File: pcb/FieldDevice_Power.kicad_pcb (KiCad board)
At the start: 2 copper layers, 22.9 x 20.6 mm, 12 parts, among them U1 LM2621

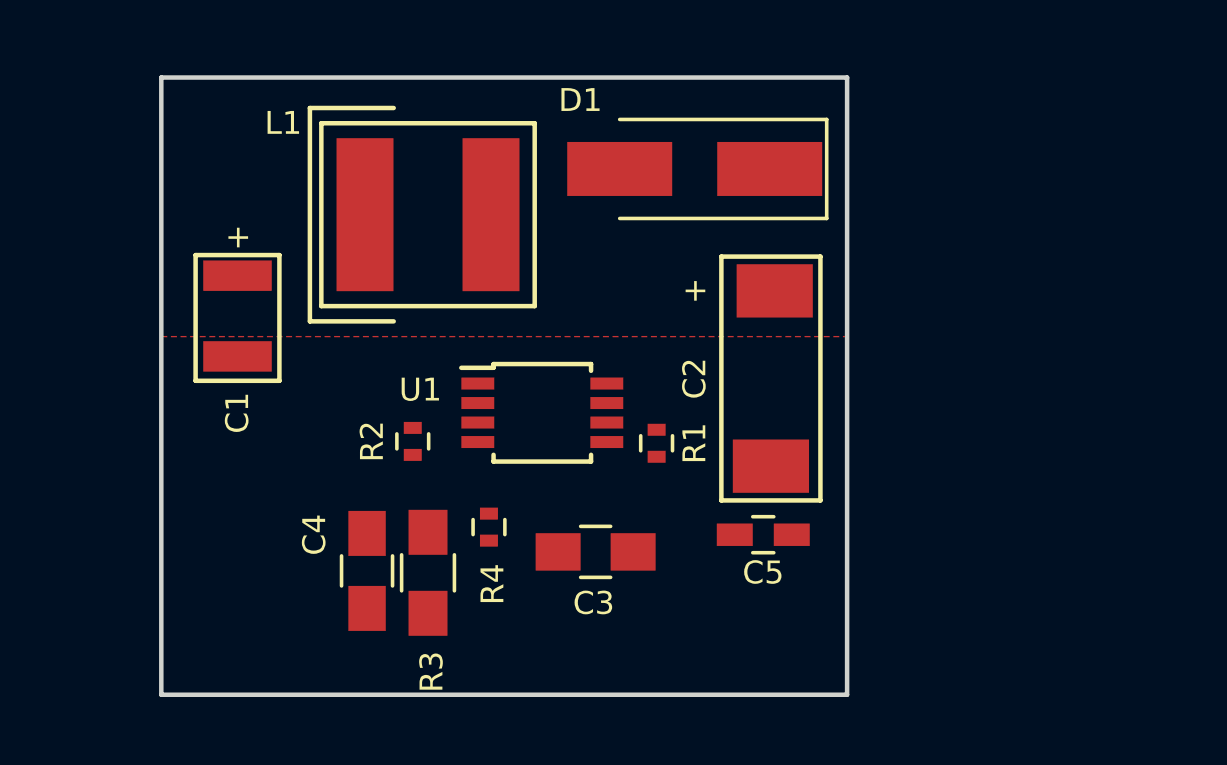
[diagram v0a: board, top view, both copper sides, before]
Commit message: Added the pin headers for Vin and Vout
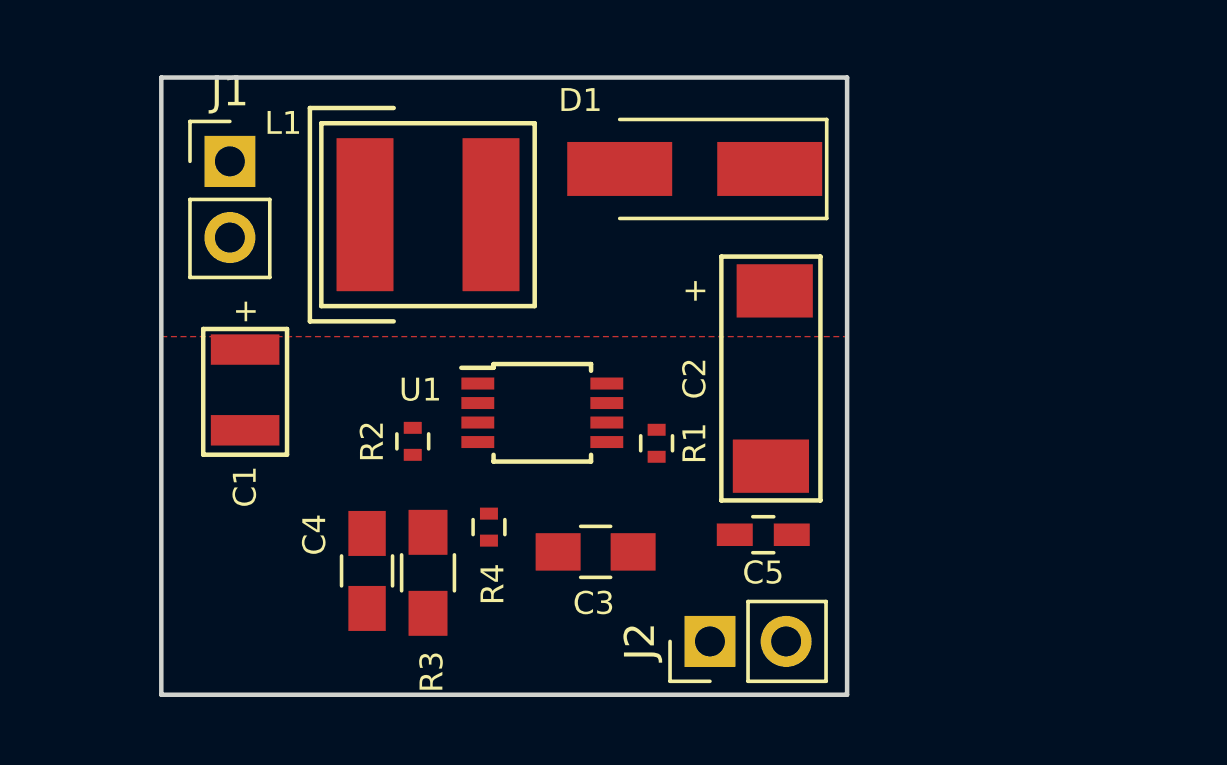
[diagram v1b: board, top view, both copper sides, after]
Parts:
- added J1: Vin, Pin_Headers:Pin_Header_Straight_1x02_Pitch2.54mm, F.Cu at (168.1, 98.8)
- added J2: Vout, Pin_Headers:Pin_Header_Straight_1x02_Pitch2.54mm, F.Cu at (184.2, 114.8)
- moved C1 2.48 mm to (168.7, 106.4)
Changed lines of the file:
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@@
 (kicad_pcb (version 4) (host pcbnew 4.0.7)
   (general
-    (links 23)
-    (no_connects 17)
-    (area 0 0 0 0)
+    (links 27)
+    (no_connects 22)
+    (area 165.786999 95.936999 188.797001 116.661001)
     (thickness 1.6)
     (drawings 4)
     (tracks 0)
     (zones 0)
-    (modules 12)
+    (modules 14)
     (nets 8)
   )
@@
     (pad_to_mask_clearance 0.2)
     (aux_axis_origin 0 0)
-    (visible_elements FFFEFF7F)
+    (visible_elements 7FFFFFFF)
     (pcbplotparams
       (layerselection 0x00030_80000001)
@@
   )
   (module FieldDevice_Power:Capacitor_1411 (layer F.Cu)
-    (at 168.402 103.9622 270)
+    (at 168.656 106.426 270)
     (fp_text reference C1 (at 3.2258 0 270) (layer F.SilkS)
       (effects (font (size 0.762 0.762) (thickness 0.127)))
@@
       (at (xyz 0 0 0))
       (scale (xyz 1 1 1))
+      (rotate (xyz 0 0 0))
+    )
+  )
+  (module Pin_Headers:Pin_Header_Straight_1x02_Pitch2.54mm (layer F.Cu)
+    (at 168.148 98.806)
+    (descr "Through hole straight pin header, 1x02, 2.54mm pitch, single row")
+    (tags "Through hole pin header THT 1x02 2.54mm single row")
+    (fp_text reference J1 (at 0 -2.33) (layer F.SilkS)
+      (effects (font (size 1 1) (thickness 0.15)))
+    )
+    (fp_text value Vin (at 0 4.87) (layer F.Fab)
+      (effects (font (size 1 1) (thickness 0.15)))
+    )
+    (fp_line (start -0.635 -1.27) (end 1.27 -1.27) (layer F.Fab) (width 0.1))
+    (fp_line (start 1.27 -1.27) (end 1.27 3.81) (layer F.Fab) (width 0.1))
+    (fp_line (start 1.27 3.81) (end -1.27 3.81) (layer F.Fab) (width 0.1))
+    (fp_line (start -1.27 3.81) (end -1.27 -0.635) (layer F.Fab) (width 0.1))
+    (fp_line (start -1.27 -0.635) (end -0.635 -1.27) (layer F.Fab) (width 0.1))
+    (fp_line (start -1.33 3.87) (end 1.33 3.87) (layer F.SilkS) (width 0.12))
+    (fp_line (start -1.33 1.27) (end -1.33 3.87) (layer F.SilkS) (width 0.12))
+    (fp_line (start 1.33 1.27) (end 1.33 3.87) (layer F.SilkS) (width 0.12))
+    (fp_line (start -1.33 1.27) (end 1.33 1.27) (layer F.SilkS) (width 0.12))
+    (fp_line (start -1.33 0) (end -1.33 -1.33) (layer F.SilkS) (width 0.12))
+    (fp_line (start -1.33 -1.33) (end 0 -1.33) (layer F.SilkS) (width 0.12))
+    (fp_line (start -1.8 -1.8) (end -1.8 4.35) (layer F.CrtYd) (width 0.05))
+    (fp_line (start -1.8 4.35) (end 1.8 4.35) (layer F.CrtYd) (width 0.05))
+    (fp_line (start 1.8 4.35) (end 1.8 -1.8) (layer F.CrtYd) (width 0.05))
+    (fp_line (start 1.8 -1.8) (end -1.8 -1.8) (layer F.CrtYd) (width 0.05))
+    (fp_text user %R (at 0 1.27 90) (layer F.Fab)
+      (effects (font (size 1 1) (thickness 0.15)))
+    )
+    (pad 1 thru_hole rect (at 0 0) (size 1.7 1.7) (drill 1) (layers *.Cu *.Mask)
+      (net 2 /Vin))
+    (pad 2 thru_hole oval (at 0 2.54) (size 1.7 1.7) (drill 1) (layers *.Cu *.Mask)
+      (net 1 GND))
+    (model ${KISYS3DMOD}/Pin_Headers.3dshapes/Pin_Header_Straight_1x02_Pitch2.54mm.wrl
+      (at (xyz 0 0 0))
+      (scale (xyz 1 1 1))
+      (rotate (xyz 0 0 0))
+    )
+  )
+  (module Pin_Headers:Pin_Header_Straight_1x02_Pitch2.54mm (layer F.Cu)
+    (at 184.15 114.808 90)
+    (descr "Through hole straight pin header, 1x02, 2.54mm pitch, single row")
+    (tags "Through hole pin header THT 1x02 2.54mm single row")
+    (fp_text reference J2 (at 0 -2.33 90) (layer F.SilkS)
+      (effects (font (size 1 1) (thickness 0.15)))
+    )
+    (fp_text value Vout (at 0 4.87 90) (layer F.Fab)
+      (effects (font (size 1 1) (thickness 0.15)))
+    )
+    (fp_line (start -0.635 -1.27) (end 1.27 -1.27) (layer F.Fab) (width 0.1))
+    (fp_line (start 1.27 -1.27) (end 1.27 3.81) (layer F.Fab) (width 0.1))
+    (fp_line (start 1.27 3.81) (end -1.27 3.81) (layer F.Fab) (width 0.1))
+    (fp_line (start -1.27 3.81) (end -1.27 -0.635) (layer F.Fab) (width 0.1))
+    (fp_line (start -1.27 -0.635) (end -0.635 -1.27) (layer F.Fab) (width 0.1))
+    (fp_line (start -1.33 3.87) (end 1.33 3.87) (layer F.SilkS) (width 0.12))
+    (fp_line (start -1.33 1.27) (end -1.33 3.87) (layer F.SilkS) (width 0.12))
+    (fp_line (start 1.33 1.27) (end 1.33 3.87) (layer F.SilkS) (width 0.12))
+    (fp_line (start -1.33 1.27) (end 1.33 1.27) (layer F.SilkS) (width 0.12))
+    (fp_line (start -1.33 0) (end -1.33 -1.33) (layer F.SilkS) (width 0.12))
+    (fp_line (start -1.33 -1.33) (end 0 -1.33) (layer F.SilkS) (width 0.12))
+    (fp_line (start -1.8 -1.8) (end -1.8 4.35) (layer F.CrtYd) (width 0.05))
+    (fp_line (start -1.8 4.35) (end 1.8 4.35) (layer F.CrtYd) (width 0.05))
+    (fp_line (start 1.8 4.35) (end 1.8 -1.8) (layer F.CrtYd) (width 0.05))
+    (fp_line (start 1.8 -1.8) (end -1.8 -1.8) (layer F.CrtYd) (width 0.05))
+    (fp_text user %R (at 0 1.27 180) (layer F.Fab)
+      (effects (font (size 1 1) (thickness 0.15)))
+    )
+    (pad 1 thru_hole rect (at 0 0 90) (size 1.7 1.7) (drill 1) (layers *.Cu *.Mask)
+      (net 3 /Vout))
+    (pad 2 thru_hole oval (at 0 2.54 90) (size 1.7 1.7) (drill 1) (layers *.Cu *.Mask)
+      (net 1 GND))
+    (model ${KISYS3DMOD}/Pin_Headers.3dshapes/Pin_Header_Straight_1x02_Pitch2.54mm.wrl
+      (at (xyz 0 0 0))
+      (scale (xyz 1 1 1))

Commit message: Completed the layout and parts decisions
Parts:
- added G***: LOGO, FieldDevice_Power:MyBasic_rounded_50_1, B.Cu at (180.8, 100.5)
- added G***: LOGO, FieldDevice_Power:MyBasic_rounded_50_1, F.Cu at (170.2, 111.6)
- added G***: LOGO, FieldDevice_Power:KiCad-Logo, F.Cu at (187.6, 114.7)
- added REF***: KiCad-Logo2_6mm_SilkScreen, Symbols:KiCad-Logo2_6mm_SilkScreen, B.Cu at (180.8, 113.4)
- added Tp1: VinTest, Pin_Headers:Pin_Header_Straight_1x02_Pitch2.54mm, F.Cu at (164.3, 111.3)
- added Tp2: VoutTest, Pin_Headers:Pin_Header_Straight_1x02_Pitch2.54mm, F.Cu at (196.8, 111.3)
- added Tp3: IinTest, Pin_Headers:Pin_Header_Straight_1x02_Pitch2.54mm, F.Cu at (166.9, 106.7)
- added Tp4: IoutTest, Pin_Headers:Pin_Header_Straight_1x02_Pitch2.54mm, F.Cu at (196.8, 106.7)
- C1: footprint FieldDevice_Power:Capacitor_1411 -> Capacitors_Tantalum_SMD:CP_Tantalum_Case-B_EIA-3528-21_Hand
- C2: value 68μF -> 100μF; footprint FieldDevice_Power:Capacitor_2917 -> Capacitors_Tantalum_SMD:CP_Tantalum_Case-D_EIA-7343-31_Hand
- C3: value 100nF 16V -> 1uF 16V
- L1: footprint FieldDevice_Power:INDUCTOR_VLS6045EX-6R8M -> FieldDevice_Power:INDUCTOR_1255AY-6R8M=P3
- R1: value 500Ω -> 48.7Ω
- R2: value 200kΩ -> 357kΩ E96, 1%
- R4: value 50kΩ -> 49.9kΩ E96 1%
- moved J2 19.8 mm to (196.8, 99.6), turned to 0 degrees
- moved C5 7.65 mm to (193.5, 110.6), turned to 90 degrees
- moved J1 5.04 mm to (164.3, 102.1), turned to 180 degrees
- moved R2 5.03 mm to (178.8, 110.2), turned to 270 degrees
- moved C1 4.32 mm to (171.6, 103.2)
- moved R4 3.99 mm to (174.8, 107.6), turned to 270 degrees
- moved L1 3.59 mm to (178.3, 100.1)
- moved D1 3.20 mm to (186.8, 98.7)
- moved C2 2.77 mm to (189.0, 106.8)
- moved C3 2.58 mm to (182.4, 110.2)
- moved C4 2.43 mm to (175.0, 111.6)
- moved R3 2.41 mm to (177.0, 111.8)
- moved R1 1.27 mm to (183.1, 107.2)
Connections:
- C1 pad 1: /Vin -> /Vin1
- C2 pad 1: /Vout -> /Vout1
- C4 pad 1: /Vout -> /Vout1
- C5 pad 2: /Vout -> /Vout1
- D1 pad 1: /Vout -> /Vout1
- L1 pad 1: /Vin -> /Vin1
- R1 pad 2: /Vout -> /Vout1
- R3 pad 1: /Vout -> /Vout1
- U1 pad 7: /Vout -> /Vout1
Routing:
- net GND: track 0.00 -> 46.9 mm
- net /Vout1: track 0.00 -> 23.6 mm, vias 0 -> 2
- net Net-(C3-Pad2): track 0.00 -> 15.3 mm
- net /Vout: track 0.00 -> 13.0 mm
- net /Vin: track 0.00 -> 8.38 mm
- net Net-(C4-Pad2): track 0.00 -> 6.23 mm
- net Net-(R2-Pad1): track 0.00 -> 3.68 mm
- net /Vin1: track 0.00 -> 0.89 mm
- added copper zone on F.Cu, net /Vin1
- added copper zone on F.Cu, net /Vout1
- added copper zone on F.Cu, net Net-(D1-Pad2)
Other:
- board size 22.9 x 20.6 mm -> 36.1 x 20.3 mm
- net class Default: clearance 0.2 -> 0.1524; trace_width 0.25 -> 0.1524; via_dia 0.6 -> 0.6858; via_drill 0.4 -> 0.3302
- rule pad_to_mask_clearance: 0.2 -> 0
- rule trace_clearance: 0.2 -> 0.1524
- rule trace_min: 0.2 -> 0.1524
- rule via_min_drill: 0.3 -> 0.3302
- rule via_min_size: 0.4 -> 0.6858
- board text added: "+ 3V7 Vin"
- board text added: "+ 5V Out"
- board text added: "+ I-in Tp"
- board text added: "+ I-out Tp"
- board text added: "Field Device Power LM2621 2L_1"
- board text added: "V-in Tp +"
- board text added: "V-out Tp +"

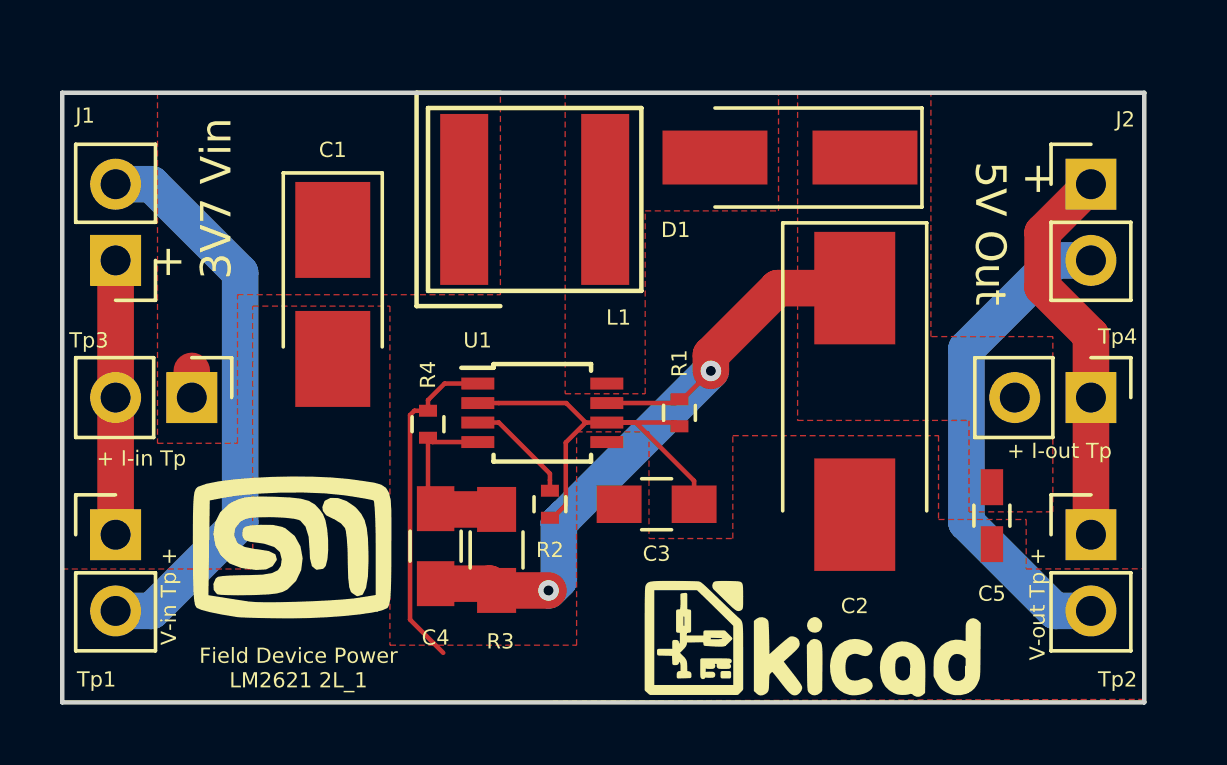
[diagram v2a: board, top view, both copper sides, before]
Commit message: Updated a replacement for R4
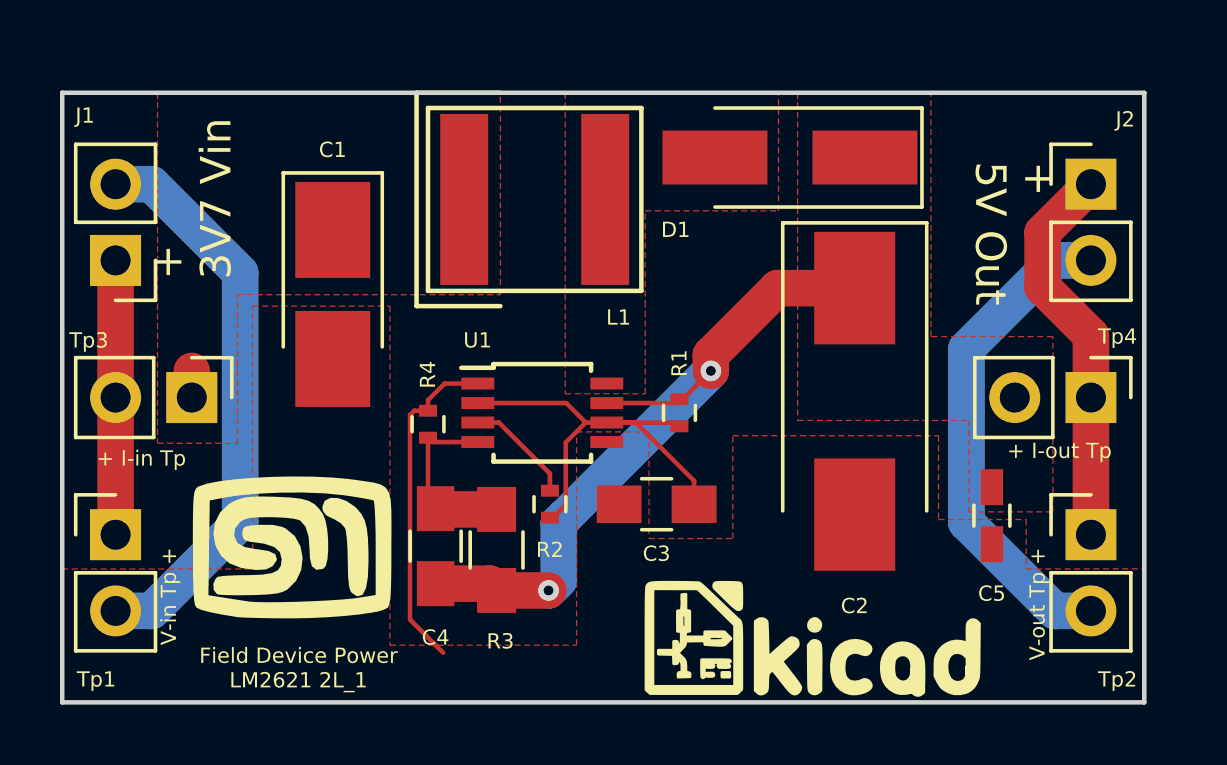
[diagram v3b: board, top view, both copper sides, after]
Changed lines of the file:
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@@
         (xy 168.91 103.632) (xy 173.482 103.632) (xy 173.482 114.935) (xy 179.705 114.935) (xy 179.705 107.823)
         (xy 182.118 107.823) (xy 182.118 111.379) (xy 184.912 111.379) (xy 184.912 107.95) (xy 191.77 107.95)
-        (xy 191.77 110.744) (xy 194.691 110.744) (xy 194.691 112.395) (xy 198.628 112.387825) (xy 198.628 116.739906)
+        (xy 191.77 110.744) (xy 194.691 110.744) (xy 194.691 112.395) (xy 198.628 112.387825) (xy 198.628 116.84)
         (xy 162.56 116.84) (xy 162.56 112.395) (xy 168.91 112.395)
       )
